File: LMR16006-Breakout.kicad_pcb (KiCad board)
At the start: 2 copper layers, 21 x 21 mm, 17 parts, among them P1 CONN_01X04, U1 LMR16006

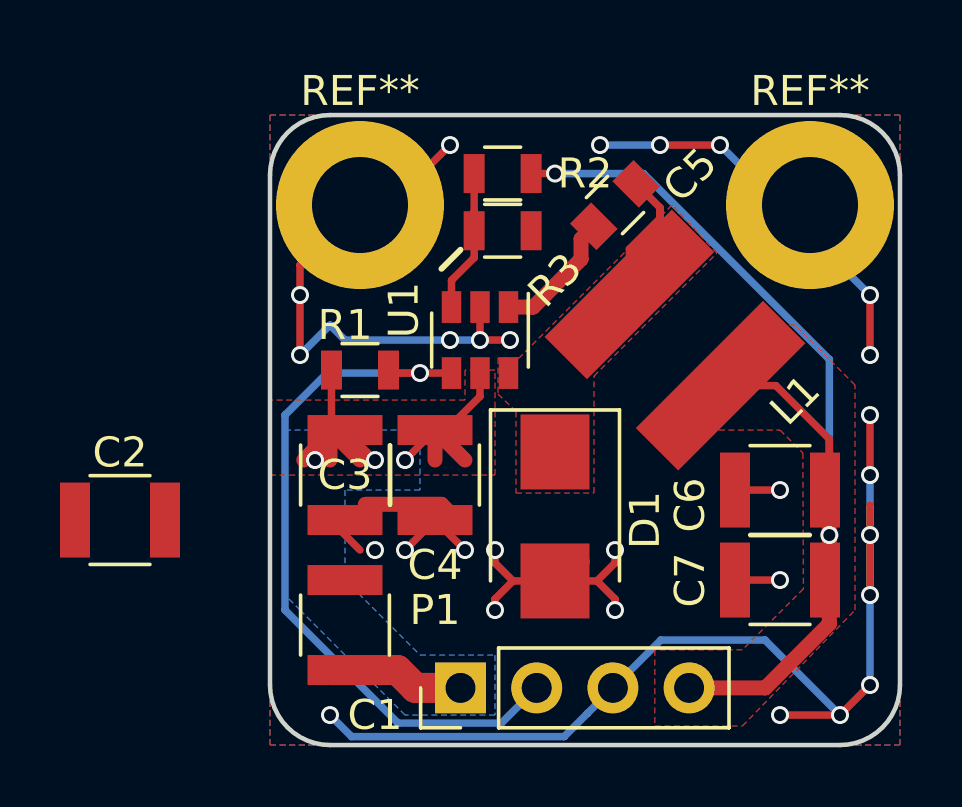
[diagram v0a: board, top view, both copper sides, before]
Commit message: update 3d view, some tweaks, silkscreen
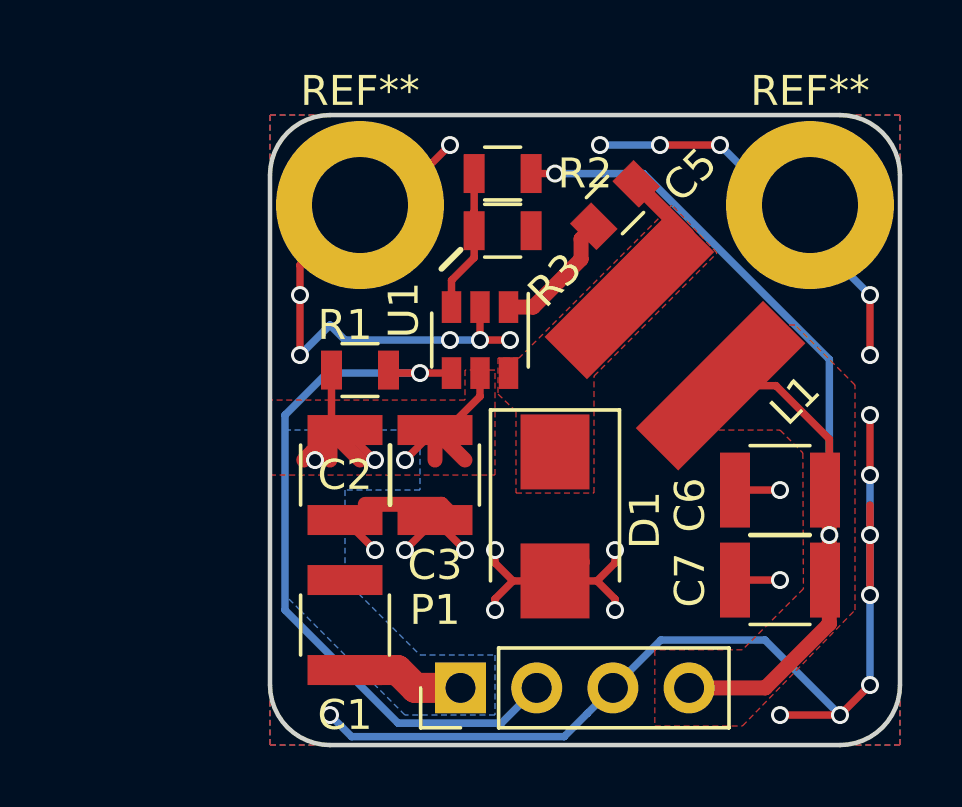
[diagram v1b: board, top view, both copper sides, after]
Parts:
- removed C4: 1µF, Capacitors_SMD:C_1210
- moved C2 7.65 mm to (122.5, 101.0), turned to 270 degrees
- moved C3 3.00 mm to (125.5, 101.0)
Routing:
- net Net-(C5-Pad2): track 10.5 -> 9.03 mm
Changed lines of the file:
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@@
 (kicad_pcb (version 4) (host pcbnew 4.0.5)
   (general
-    (links 29)
-    (no_connects 2)
+    (links 27)
+    (no_connects 0)
     (area 119.924999 88.924999 141.075001 110.075001)
     (thickness 1.6)
     (drawings 15)
-    (tracks 146)
+    (tracks 144)
     (zones 0)
-    (modules 17)
+    (modules 16)
     (nets 8)
   )
@@
     (tags "capacitor 1210")
     (attr smd)
-    (fp_text reference C1 (at -3 1 360) (layer F.SilkS)
+    (fp_text reference C1 (at -3 0 360) (layer F.SilkS)
       (effects (font (size 1 1) (thickness 0.15)))
     )
@@
   )
   (module Capacitors_SMD:C_1210 (layer F.Cu)
-    (at 115 102.5)
-    (descr "Capacitor SMD 1210, reflow soldering, AVX (see smccp.pdf)")
-    (tags "capacitor 1210")
-    (attr smd)
-    (fp_text reference C2 (at 0 -2.25) (layer F.SilkS)
-      (effects (font (size 1 1) (thickness 0.15)))
-    )
-    (fp_text value 1µF (at 0 2.5) (layer F.Fab)
-      (effects (font (size 1 1) (thickness 0.15)))
-    )
-    (fp_text user %R (at 0 -2.25) (layer F.Fab)
-      (effects (font (size 1 1) (thickness 0.15)))
-    )
-    (fp_line (start -1.6 1.25) (end -1.6 -1.25) (layer F.Fab) (width 0.1))
-    (fp_line (start 1.6 1.25) (end -1.6 1.25) (layer F.Fab) (width 0.1))
-    (fp_line (start 1.6 -1.25) (end 1.6 1.25) (layer F.Fab) (width 0.1))
-    (fp_line (start -1.6 -1.25) (end 1.6 -1.25) (layer F.Fab) (width 0.1))
-    (fp_line (start 1 -1.48) (end -1 -1.48) (layer F.SilkS) (width 0.12))
-    (fp_line (start -1 1.48) (end 1 1.48) (layer F.SilkS) (width 0.12))
-    (fp_line (start -2.25 -1.5) (end 2.25 -1.5) (layer F.CrtYd) (width 0.05))
-    (fp_line (start -2.25 -1.5) (end -2.25 1.5) (layer F.CrtYd) (width 0.05))
-    (fp_line (start 2.25 1.5) (end 2.25 -1.5) (layer F.CrtYd) (width 0.05))
-    (fp_line (start 2.25 1.5) (end -2.25 1.5) (layer F.CrtYd) (width 0.05))
-    (pad 1 smd rect (at -1.5 0) (size 1 2.5) (layers F.Cu F.Paste F.Mask)
-      (net 1 VCC))
-    (pad 2 smd rect (at 1.5 0) (size 1 2.5) (layers F.Cu F.Paste F.Mask)
-      (net 2 GND))
-    (model Capacitors_SMD.3dshapes/C_1210.wrl
-      (at (xyz 0 0 0))
-      (scale (xyz 1 1 1))
-      (rotate (xyz 0 0 0))
-    )
-  )
-  (module Capacitors_SMD:C_1210 (layer F.Cu)
     (at 122.5 101 270)
     (descr "Capacitor SMD 1210, reflow soldering, AVX (see smccp.pdf)")
     (tags "capacitor 1210")
     (attr smd)
-    (fp_text reference C3 (at 0 0 360) (layer F.SilkS)
+    (fp_text reference C2 (at 0 0 540) (layer F.SilkS)
       (effects (font (size 1 1) (thickness 0.15)))
     )
@@
     (tags "capacitor 1210")
     (attr smd)
-    (fp_text reference C4 (at 3 0 360) (layer F.SilkS)
+    (fp_text reference C3 (at 3 0 360) (layer F.SilkS)
       (effects (font (size 1 1) (thickness 0.15)))
     )
@@
   (segment (start 124.845 108.095) (end 124.25 107.5) (width 1) (layer F.Cu) (net 1))
   (segment (start 124.25 107.5) (end 122 107.5) (width 1) (layer F.Cu) (net 1))
+  (segment (start 122.5 102.5) (end 123.5 103.5) (width 0.25) (layer F.Cu) (net 2))
+  (via (at 123.5 103.5) (size 0.6) (drill 0.4) (layers F.Cu B.Cu) (net 2))
   (segment (start 122 96) (end 122.5 96.5) (width 0.25) (layer B.Cu) (net 2))
   (segment (start 122.5 96.5) (end 126 96.5) (width 0.25) (layer B.Cu) (net 2))
@@
   (via (at 137 101.5) (size 0.6) (drill 0.4) (layers F.Cu B.Cu) (net 2))
   (via (at 121 97) (size 0.6) (drill 0.4) (layers F.Cu B.Cu) (net 2))
-  (segment (start 122 102.5) (end 123 103.5) (width 0.25) (layer F.Cu) (net 2))
-  (via (at 123.5 103.5) (size 0.6) (drill 0.4) (layers F.Cu B.Cu) (net 2))
   (segment (start 125.5 102.5) (end 126.5 103.5) (width 0.25) (layer F.Cu) (net 2))
   (via (at 126.5 103.5) (size 0.6) (drill 0.4) (layers F.Cu B.Cu) (net 2))
@@
   (segment (start 127.95 95.4) (end 128.775 95.4) (width 0.5) (layer F.Cu) (net 3))
   (segment (start 128.775 95.4) (end 130.36863 93.80637) (width 0.5) (layer F.Cu) (net 3))
-  (segment (start 131.97972 94.97972) (end 131.97972 93.465507) (width 0.25) (layer F.Cu) (net 4))
-  (segment (start 131.97972 93.465507) (end 133 92.445227) (width 0.25) (layer F.Cu) (net 4))
-  (segment (start 133 92.445227) (end 133 92.085786) (width 0.25) (layer F.Cu) (net 4))
-  (segment (start 133 92.085786) (end 133 92.5) (width 0.25) (layer F.Cu) (net 4))
-  (segment (start 132.207107 91.292893) (end 133 92.085786) (width 0.25) (layer F.Cu) (net 4))
+  (segment (start 133.914214 93.414214) (end 133.5 93.828428) (width 0.25) (layer F.Cu) (net 4))
+  (segment (start 133.914214 93) (end 133.914214 93.414214) (width 0.25) (layer F.Cu) (net 4))
+  (segment (start 132.207107 91.292893) (end 133.914214 93) (width 0.5) (layer F.Cu) (net 4))
   (segment (start 130.71 97.13) (end 131.81 96.03) (width 0.5) (layer F.Cu) (net 4))
   (segment (start 131.81 96.03) (end 131.81 94.11) (width 0.5) (layer F.Cu) (net 4))

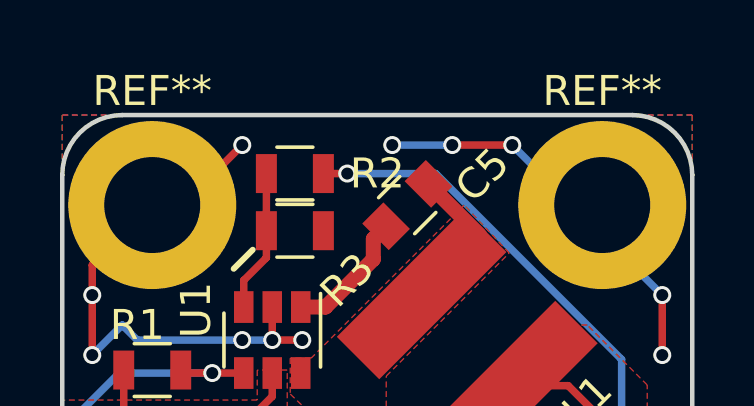
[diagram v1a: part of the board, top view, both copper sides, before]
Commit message: silkscreen placement and text
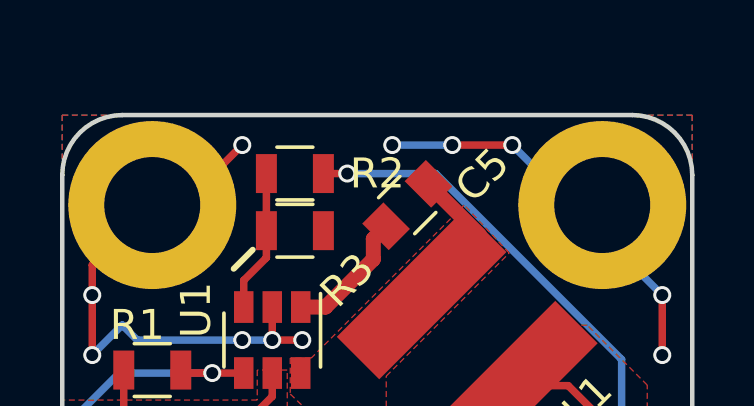
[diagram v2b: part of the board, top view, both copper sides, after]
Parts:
- removed the REF*** at (130.2, 94.8)
- added REF***: OSHW-Logo2_7.3x6mm_SilkScreen, Symbols:OSHW-Logo2_7.3x6mm_SilkScreen, B.Cu at (132.0, 92.5)
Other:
- board text added: "LMR16006 60V Buck 0,6A v1 by @kugel2"
- board text removed: "LMR16006 60V Buck converter 0,6A V1"
- board text removed: "by Florian Winkler"
